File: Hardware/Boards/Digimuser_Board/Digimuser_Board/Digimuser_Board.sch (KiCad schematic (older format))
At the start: 33 parts, among them J1 Conn_01x01, J2 Conn_01x01, J4 Conn_01x03, U1 MCP6272

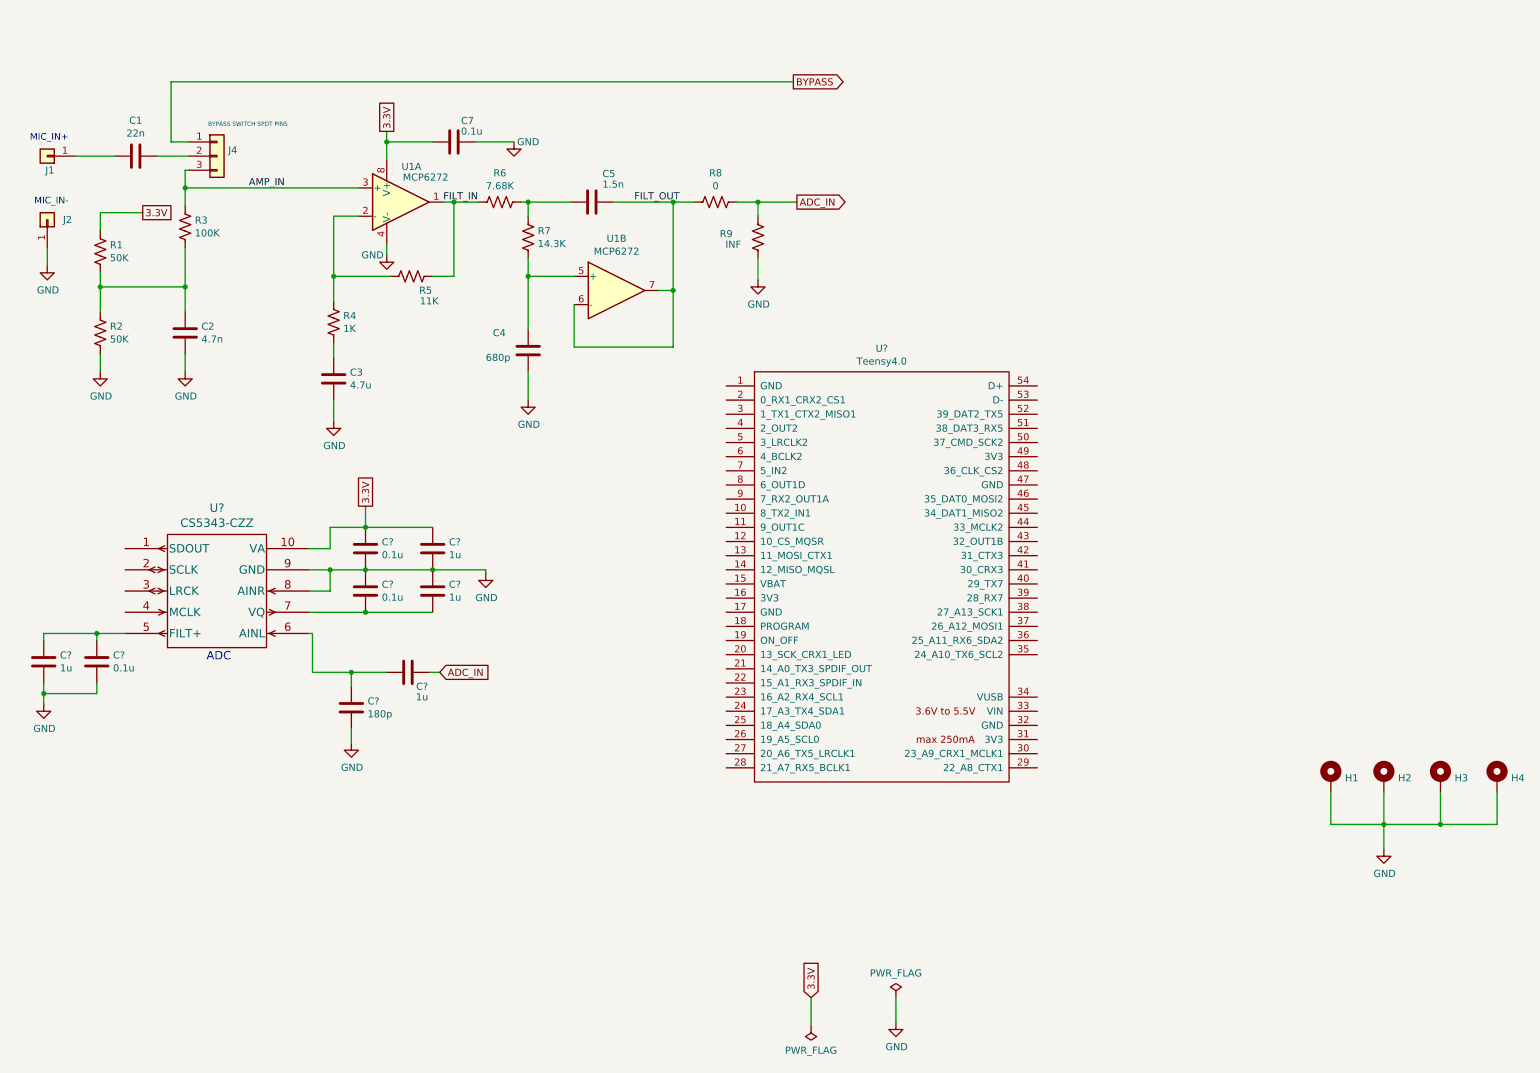
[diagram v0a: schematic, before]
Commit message: Finished the electrical connections to the ADC on the schematic.
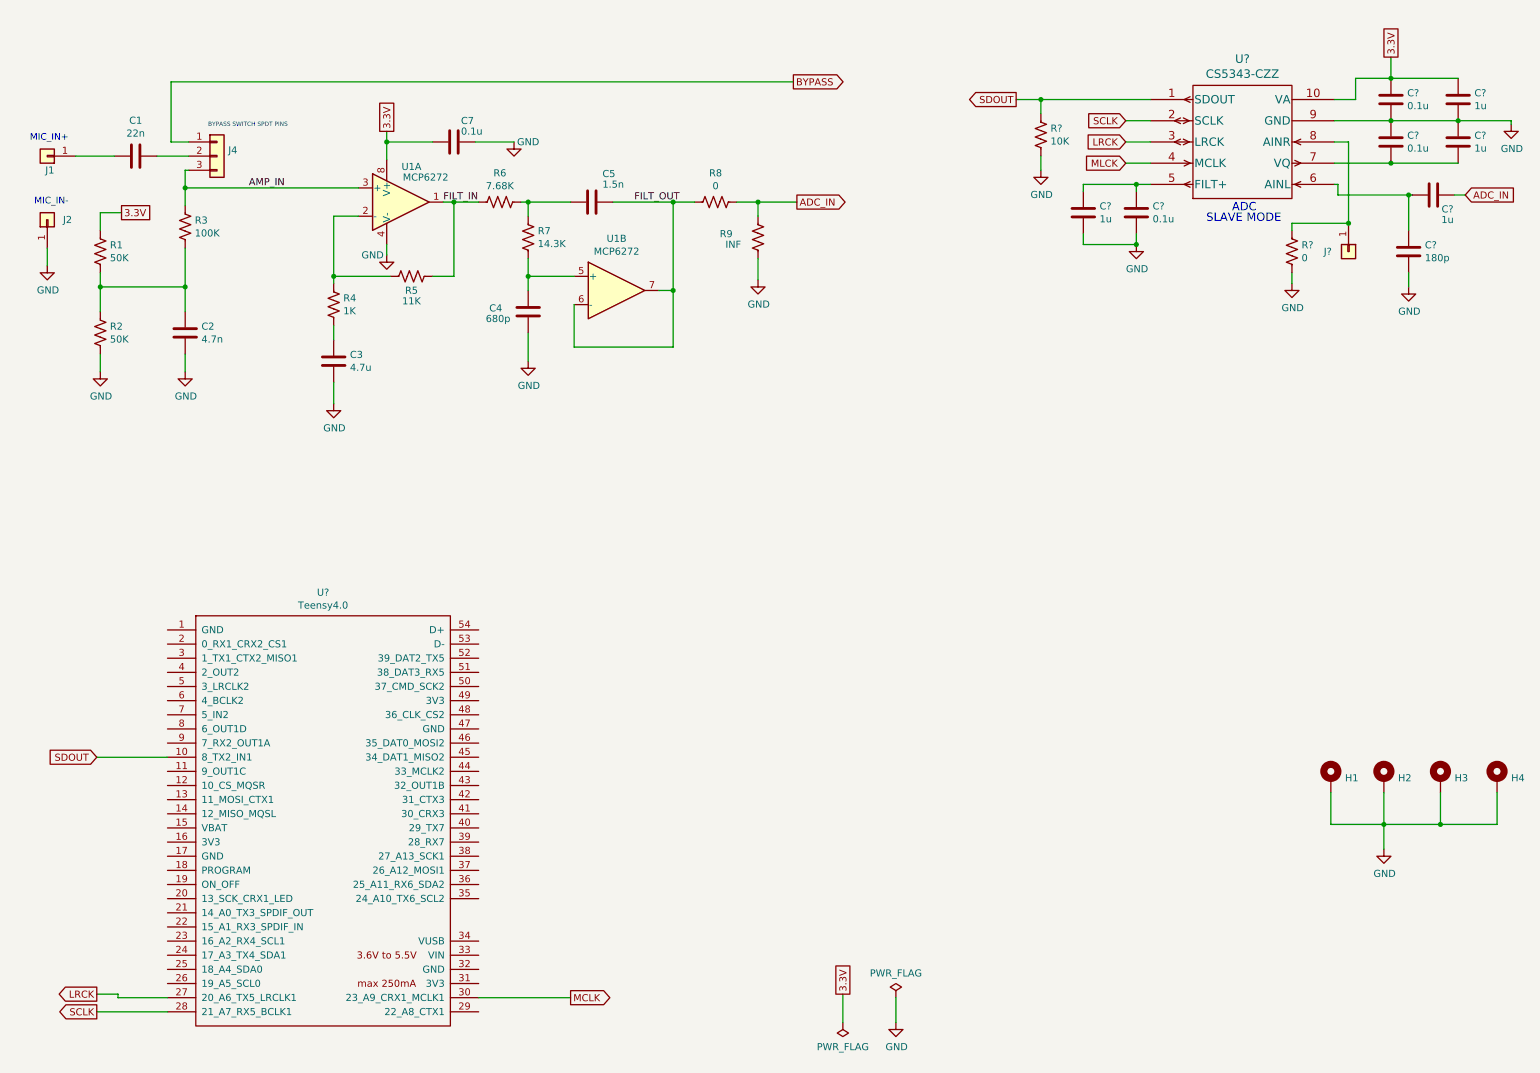
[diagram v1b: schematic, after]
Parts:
- added J?: Conn_01x01, Connector_PinSocket_2.54mm:PinSocket_1x01_P2.54mm_Vertical, symbol Connector_Generic:Conn_01x01
- added R?: 10K, Resistor_THT:R_Axial_DIN0207_L6.3mm_D2.5mm_P10.16mm_Horizontal, symbol Device:R_US
- added R?: 0, Resistor_THT:R_Axial_DIN0207_L6.3mm_D2.5mm_P10.16mm_Horizontal, symbol Device:R_US
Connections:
- net GND: now also R?.2, R?.2; no longer U?.8 (AINR)
- net SDOUT: now reaches U?.10 (8_TX2_IN1)
- net SDOUT: now also U?.1 (SDOUT), R?.1
- net LRCK: now reaches U?.27 (20_A6_TX5_LRCLK1)
- net LRCK: now also U?.3 (LRCK)
- net SCLK: now reaches U?.28 (21_A7_RX5_BCLK1)
- net SCLK: now also U?.2 (SCLK)
- net MCLK: now reaches U?.30 (23_A9_CRX1_MCLK1)
- net MLCK: now reaches U?.4 (MCLK)
- new net: J?.1 (Pin_1), R?.1, U?.8 (AINR)
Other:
- note added: "SLAVE MODE"
- moved on the sheet: C3, C4, C?, R4, U?

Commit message: Added the DAC, Output Signal Conditioner, and 5V linear regulator.
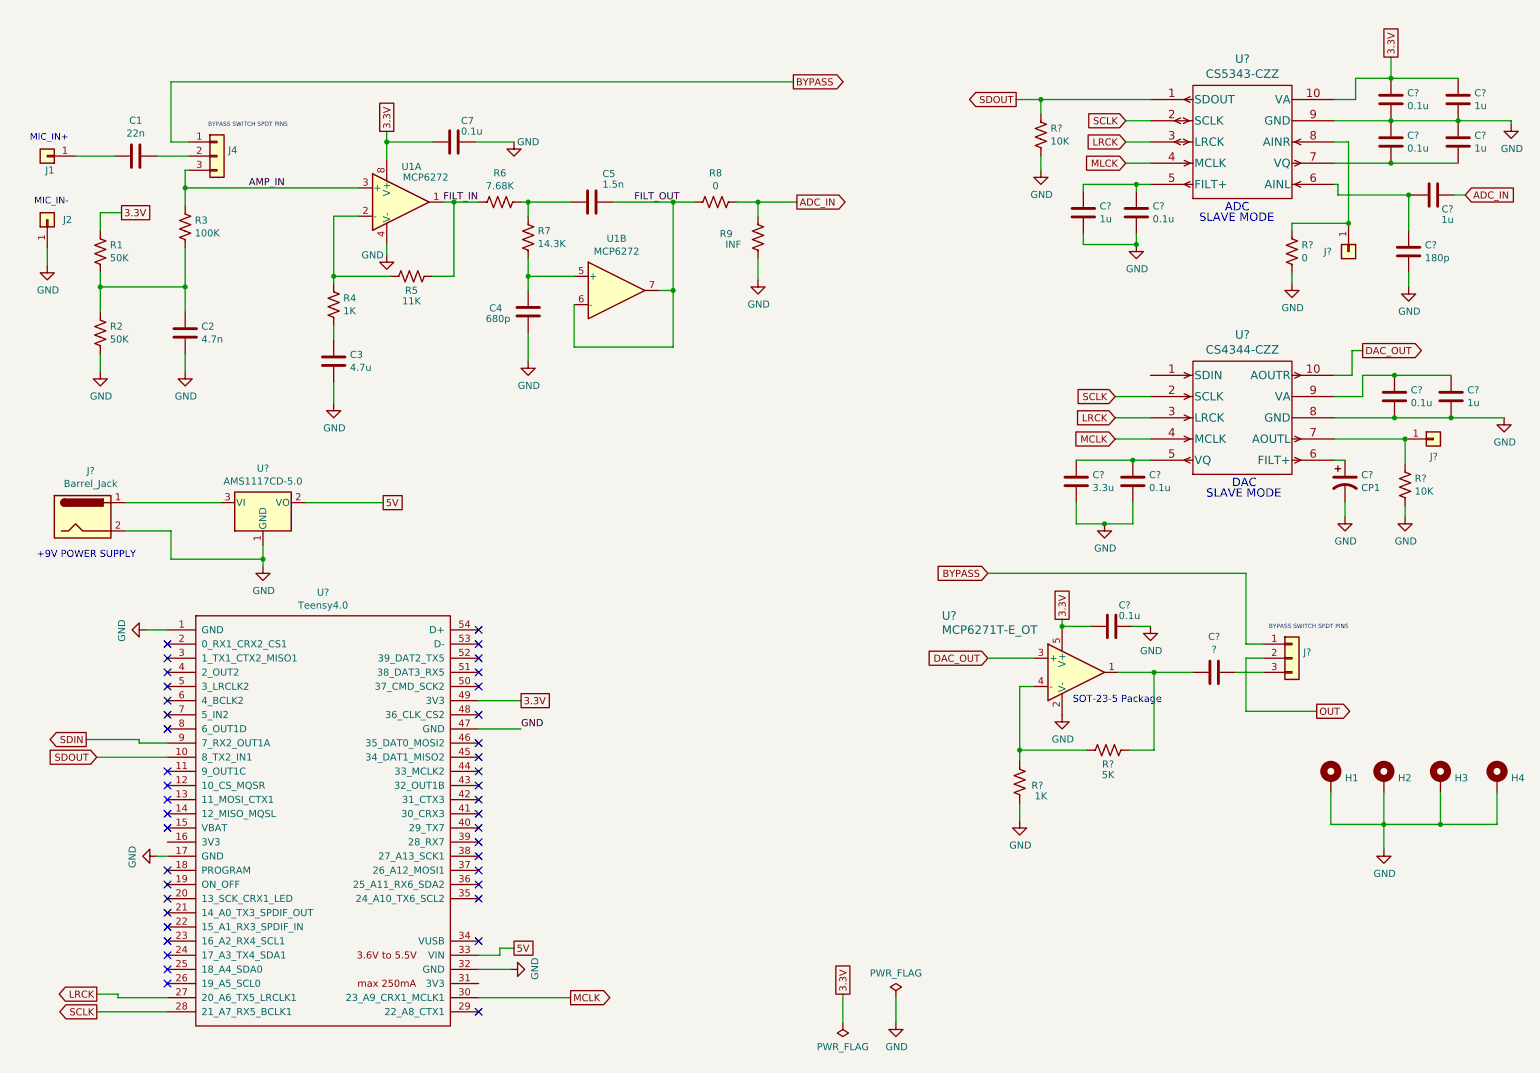
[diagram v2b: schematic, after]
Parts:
- added C? (x3): 0.1u, Capacitor_THT:C_Disc_D7.5mm_W4.4mm_P5.00mm, symbol Device:C
- added C?: 3.3u, Capacitor_THT:C_Disc_D7.5mm_W4.4mm_P5.00mm, symbol Device:C
- added C?: CP1, symbol Device:CP1
- added C?: 1u, Capacitor_THT:C_Disc_D7.5mm_W4.4mm_P5.00mm, symbol Device:C
- added C?: ?, Capacitor_THT:C_Disc_D7.5mm_W4.4mm_P5.00mm, symbol Device:C
- added J?: Conn_01x01, Connector_PinSocket_2.54mm:PinSocket_1x01_P2.54mm_Vertical, symbol Connector_Generic:Conn_01x01
- added J?: Conn_01x03, Connector_PinSocket_2.54mm:PinSocket_1x03_P2.54mm_Vertical, symbol Connector_Generic:Conn_01x03
- added J?: Barrel_Jack, symbol Connector:Barrel_Jack
- added R?: 5K, Resistor_THT:R_Axial_DIN0207_L6.3mm_D2.5mm_P10.16mm_Horizontal, symbol Device:R_US
- added R?: 1K, Resistor_THT:R_Axial_DIN0207_L6.3mm_D2.5mm_P10.16mm_Horizontal, symbol Device:R_US
- added R?: 10K, Resistor_THT:R_Axial_DIN0207_L6.3mm_D2.5mm_P10.16mm_Horizontal, symbol Device:R_US
- added U?: MCP6271T-E_OT, SOT-23-5_MC_MCH, symbol MCP6271TEOT:MCP6271T-E_OT
- added U?: CS4344-CZZ, CIR-TSSOP-10, symbol CS4344CZZ:CS4344-CZZ
- added U?: AMS1117CD-5.0, Package_TO_SOT_SMD:TO-252-3_TabPin2, symbol Regulator_Linear:AMS1117CD-5.0
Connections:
- net 3.3V: now also U?.49 (3V3), C?.2, U?.5 (V+)
- net BYPASS: now also J?.1 (Pin_1)
- net GND: now also U?.1 (GND), U?.17 (GND), U?.32 (GND), U?.47 (GND), C?.1, C?.2, C?.2, C?.2, C?.2, C?.2, J?.2, R?.1, R?.2, U?.1 (GND), U?.2 (V-), U?.8 (GND)
- net LRCK: now also U?.3 (LRCK)
- net MCLK: now also U?.4 (MCLK)
- net SCLK: now also U?.2 (SCLK)
- net 5V: now reaches U?.33 (VIN)
- net 5V: now also U?.2 (VO)
- net SDIN: now reaches U?.9 (7_RX2_OUT1A)
- new net: C?.2, R?.1, U?.1
- new net: R?.2, R?.2, U?.4 (-)
- new net: C?.1, C?.1, U?.5 (VQ)
- new net: C?.1, U?.6 (FILT+)
- new net: J?.1 (Pin_1), R?.1, U?.7 (AOUTL)
- new net: C?.1, C?.1, U?.9 (VA)
- new net: C?.1, J?.3 (Pin_3)
- new net: J?.1, U?.3 (VI)
- new net DAC_OUT: U?.10 (AOUTR), U?.3 (+)
- new net OUT: J?.2 (Pin_2)
- no-connect marks 0 -> 41
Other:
- note added: "+9V POWER SUPPLY"
- note added: "DAC\n"
- note added: "SOT-23-5 Package"

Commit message: Added the rotary switch and slider pot to the schematic. Created custom symbol for the rotary switch.
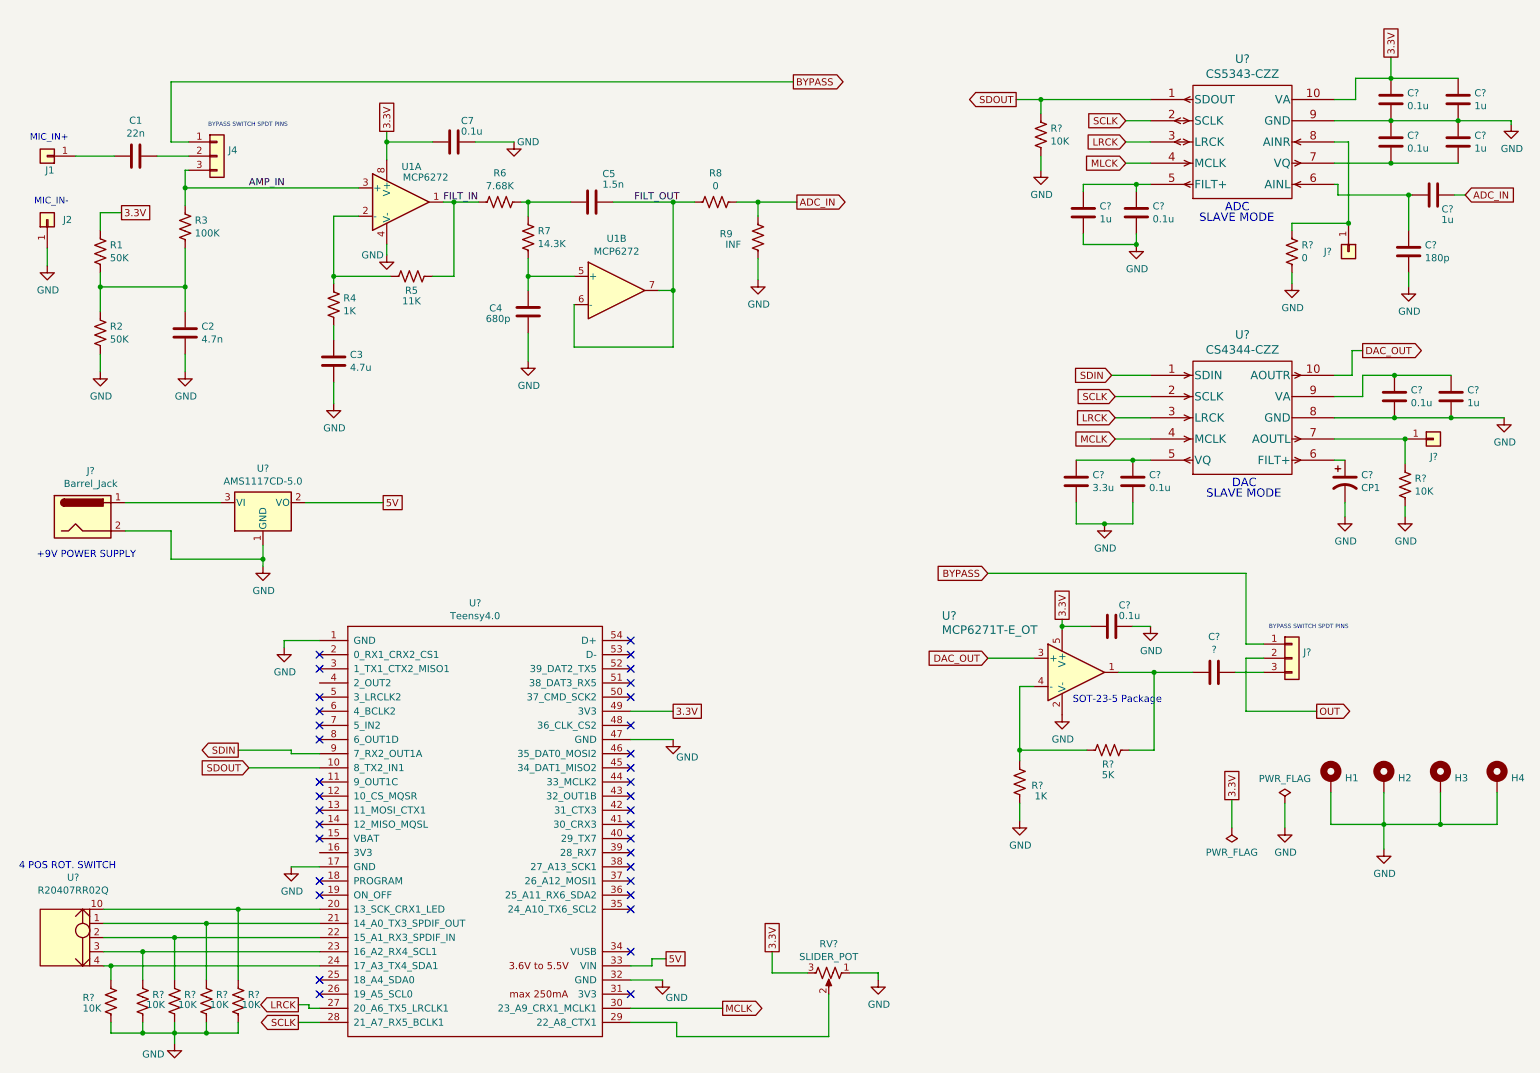
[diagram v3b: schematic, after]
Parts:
- added R? (x5): 10K, Resistor_THT:R_Axial_DIN0207_L6.3mm_D2.5mm_P10.16mm_Horizontal, symbol Device:R_US
- added RV?: SLIDER_POT, symbol Device:R_POT_US
- added U?: R20407RR02Q, symbol ‎R20407RR02Q‎_ROT_SWITCH:R20407RR02Q
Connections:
- net 3.3V: now also RV?.3
- net GND: now also R?.2, R?.2, R?.2, R?.2, R?.2, RV?.1
- net SDIN: now also U?.1 (SDIN)
- net at U?.20 (13_SCK_CRX1_LED): now also R?.1, U?.10
- net at U?.21 (14_A0_TX3_SPDIF_OUT): now also R?.1, U?.1
- net at U?.22 (15_A1_RX3_SPDIF_IN): now also R?.1, U?.2
- net at U?.23 (16_A2_RX4_SCL1): now also R?.1, U?.3
- net at U?.24 (17_A3_TX4_SDA1): now also R?.1, U?.4
- net at U?.29 (22_A8_CTX1): now also RV?.2
- no-connect marks 41 -> 35
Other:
- note added: "4 POS ROT. SWITCH"
- moved on the sheet: U?
